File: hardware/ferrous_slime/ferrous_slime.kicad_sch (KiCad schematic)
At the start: 53 parts, among them J1 IMU_Connector, J2 Unused_IO, J3 Battery_Connector, J4 USB_C_Receptacle_USB2.0, Q1 CJ2305, SW1 SW_PWR, U1 BNO/MPU/ICM_Break, U2 ESP32-C3-MINI-1, U3 TP4056, U4 M3406, Y1 32.768Hz

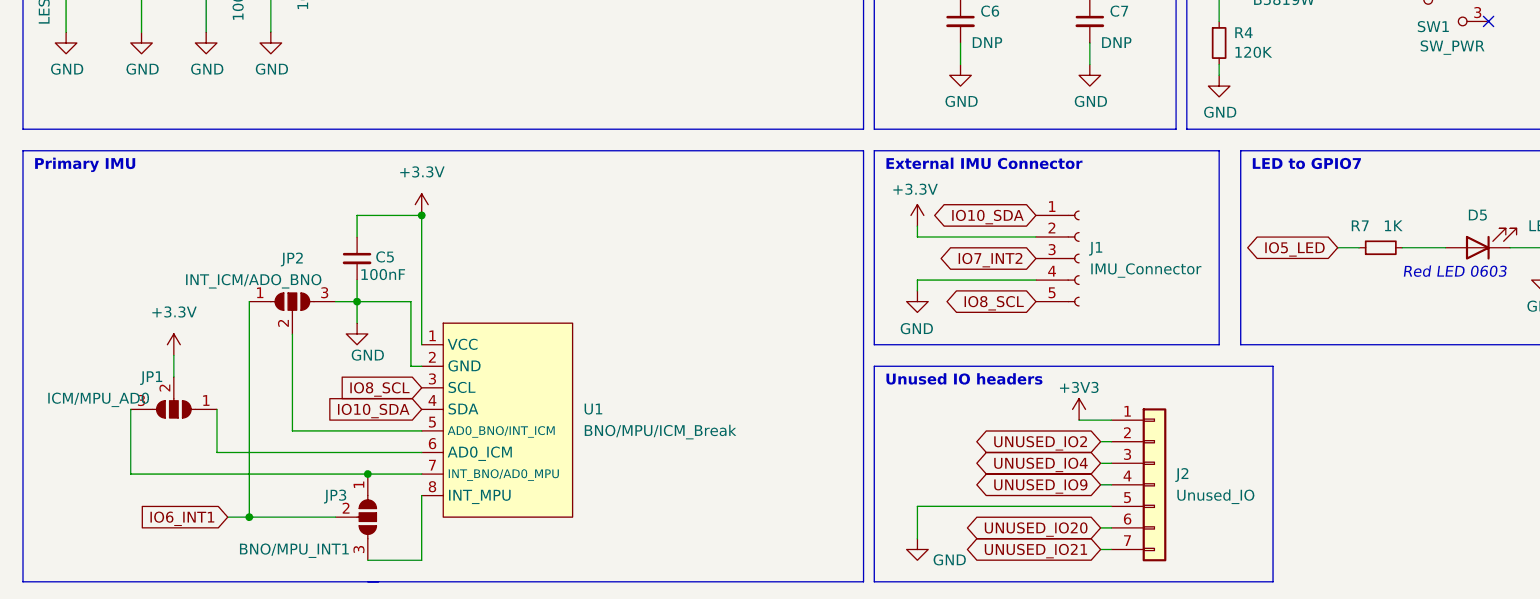
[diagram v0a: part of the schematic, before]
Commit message: Updated PCB to add second power pin
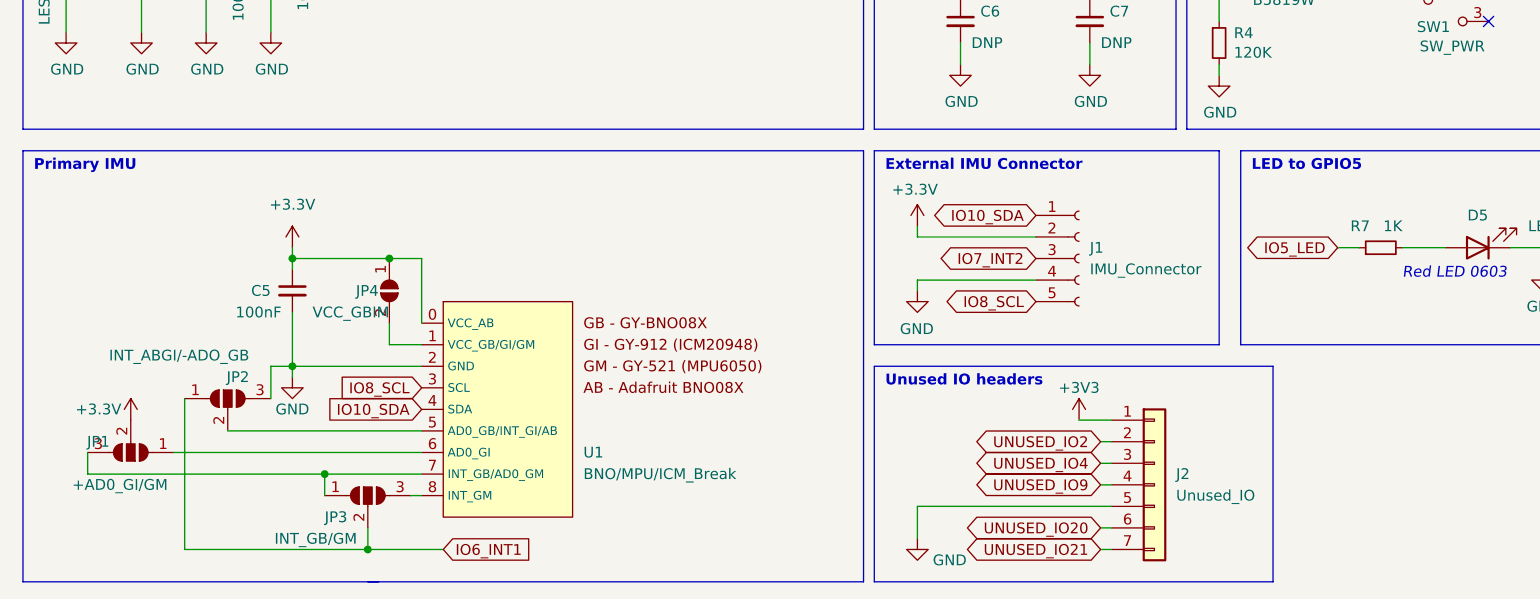
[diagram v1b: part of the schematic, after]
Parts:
- added JP4: VCC_GBIM, symbol Jumper:SolderJumper_2_Open
- JP1: value ICM/MPU_AD0 -> +AD0_GI/GM
- JP2: value INT_ICM/ADO_BNO -> INT_ABGI/-ADO_GB
- JP3: value BNO/MPU_INT1 -> INT_GB/GM
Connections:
- net +3V3: now also U1.0 (VCC_AB), JP4.1 (A); no longer U1.1 (VCC)
- new net: JP4.2 (B), U1.1 (VCC_GB/GI/GM)
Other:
- note added: "LED to GPIO5"
- note removed: "LED to GPIO7"
- moved on the sheet: C5, JP1, JP2, JP3

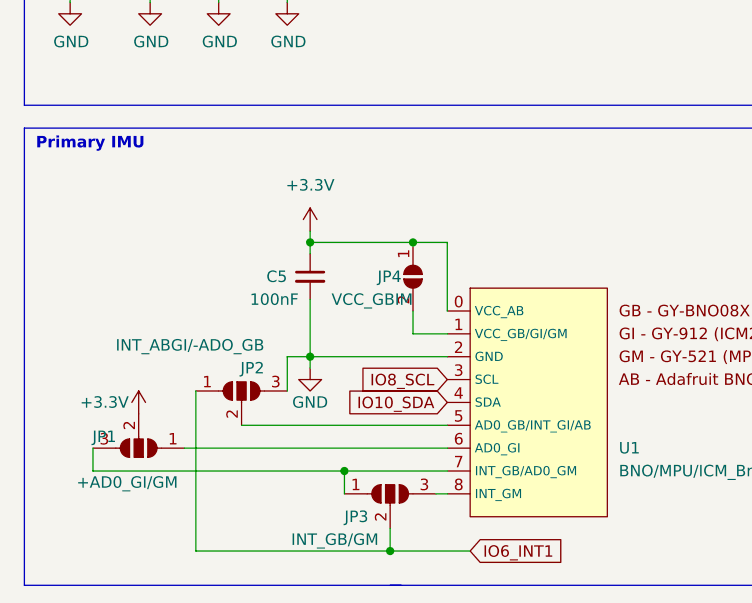
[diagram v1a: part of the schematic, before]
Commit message: Added adafruit bno to footprint
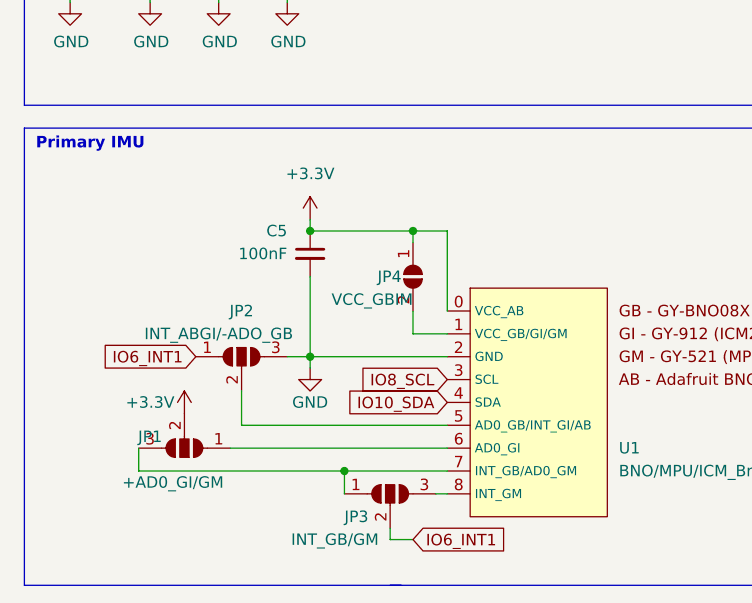
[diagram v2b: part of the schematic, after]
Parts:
- U1: footprint slimevr_pcb:BNO_MPU_ICM_Breakout -> slimevr_pcb:AB_GB_GM_GI_Breakout
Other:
- moved on the sheet: C5, JP1, JP2

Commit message: Finished pcb for ferrous_slime v0.2.0
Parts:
- D3: value LED_CHRG -> CHRG
- D4: value LED_FULL -> FULL
- D5: value LED -> LED_IO5
- JP4: footprint (none) -> Jumper:SolderJumper-2_P1.3mm_Open_RoundedPad1.0x1.5mm
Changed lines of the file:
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@@
   (title_block
     (title "ferrous_slime")
-    (date "2022-03-15")
+    (date "2022-10-11")
     (rev "v0.2.0")
     (company "github.com/thebutlah/slimevr_pcb")
@@
     (in_bom yes) (on_board yes)
     (property "Reference" "D5" (id 0) (at 185.42 121.92 0))
-    (property "Value" "LED" (id 1) (at 193.04 123.19 0))
+    (property "Value" "LED_IO5" (id 1) (at 191.77 121.92 0))
     (property "Footprint" "LED_SMD:LED_0603_1608Metric" (id 2) (at 185.42 125.73 0)
       (effects (font (size 1.27 1.27)) hide)
@@
       (effects (font (size 1.27 1.27)) (justify right))
     )
-    (property "Footprint" "" (id 2) (at 57.15 130.81 0)
+    (property "Footprint" "Jumper:SolderJumper-2_P1.3mm_Open_RoundedPad1.0x1.5mm" (id 2) (at 57.15 130.81 0)
       (effects (font (size 1.27 1.27)) hide)
     )
@@
     (in_bom yes) (on_board yes)
     (property "Reference" "D4" (id 0) (at 175.5021 40.5984 0))
-    (property "Value" "LED_FULL" (id 1) (at 179.07 44.45 0))
+    (property "Value" "FULL" (id 1) (at 181.61 40.64 0))
     (property "Footprint" "LED_SMD:LED_0603_1608Metric" (id 2) (at 177.8 41.91 90)
       (effects (font (size 1.27 1.27)) hide)
@@
     (in_bom yes) (on_board yes)
     (property "Reference" "D3" (id 0) (at 175.5021 35.4571 0))
-    (property "Value" "LED_CHRG" (id 1) (at 182.88 34.29 0))
+    (property "Value" "CHRG" (id 1) (at 181.61 35.56 0))
     (property "Footprint" "LED_SMD:LED_0603_1608Metric" (id 2) (at 177.8 36.83 90)
       (effects (font (size 1.27 1.27)) hide)
@@
     )
     (path "/bfab8950-194d-4203-9e99-e2292d8b3e2e"
-      (reference "D3") (unit 1) (value "LED_CHRG") (footprint "LED_SMD:LED_0603_1608Metric")
+      (reference "D3") (unit 1) (value "CHRG") (footprint "LED_SMD:LED_0603_1608Metric")
     )
     (path "/54080e1b-7a3e-4f86-8476-a3d55de881ec"
-      (reference "D4") (unit 1) (value "LED_FULL") (footprint "LED_SMD:LED_0603_1608Metric")
+      (reference "D4") (unit 1) (value "FULL") (footprint "LED_SMD:LED_0603_1608Metric")
     )
     (path "/00000000-0000-0000-0000-000061fd2211"
-      (reference "D5") (unit 1) (value "LED") (footprint "LED_SMD:LED_0603_1608Metric")
+      (reference "D5") (unit 1) (value "LED_IO5") (footprint "LED_SMD:LED_0603_1608Metric")
     )
     (path "/00000000-0000-0000-0000-0000625f4ff4"
@@
     )
     (path "/4b358e31-d2b1-4486-a811-6c8ba185f47e"
-      (reference "JP4") (unit 1) (value "VCC_GBIM") (footprint "")
+      (reference "JP4") (unit 1) (value "VCC_GBIM") (footprint "Jumper:SolderJumper-2_P1.3mm_Open_RoundedPad1.0x1.5mm")
     )
     (path "/32aeb981-ffe8-4bff-a65d-ee3788161f8a"

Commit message: ferrous_slime: v0.3.0
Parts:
- U1: value BNO/MPU/ICM_Break -> IMU_Breakout; footprint slimevr_pcb:AB_GB_GM_GI_Breakout -> slimevr_pcb:IMU_Breakout; symbol slimevr_pcb:BNO/MPU/ICM_Break -> slimevr_pcb:IMU_Breakout
- renumbered C8 to C7, C7 to C8, R3 to R2, R2 to R3
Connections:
- net +BATT: now also J3.1 (Pin_1); no longer J3.2 (Pin_2)
- net GND: now also J3.2 (Pin_2), U3.9 (EP); no longer J3.1 (Pin_1)
- net VBUS: no longer R3.2, U3.2 (PROG)
- new net: R3.2, U3.2 (PROG)
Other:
- note added: "R8 prevents ESD"
- note removed: "R12 prevents ESD"
- moved on the sheet: C7, R3

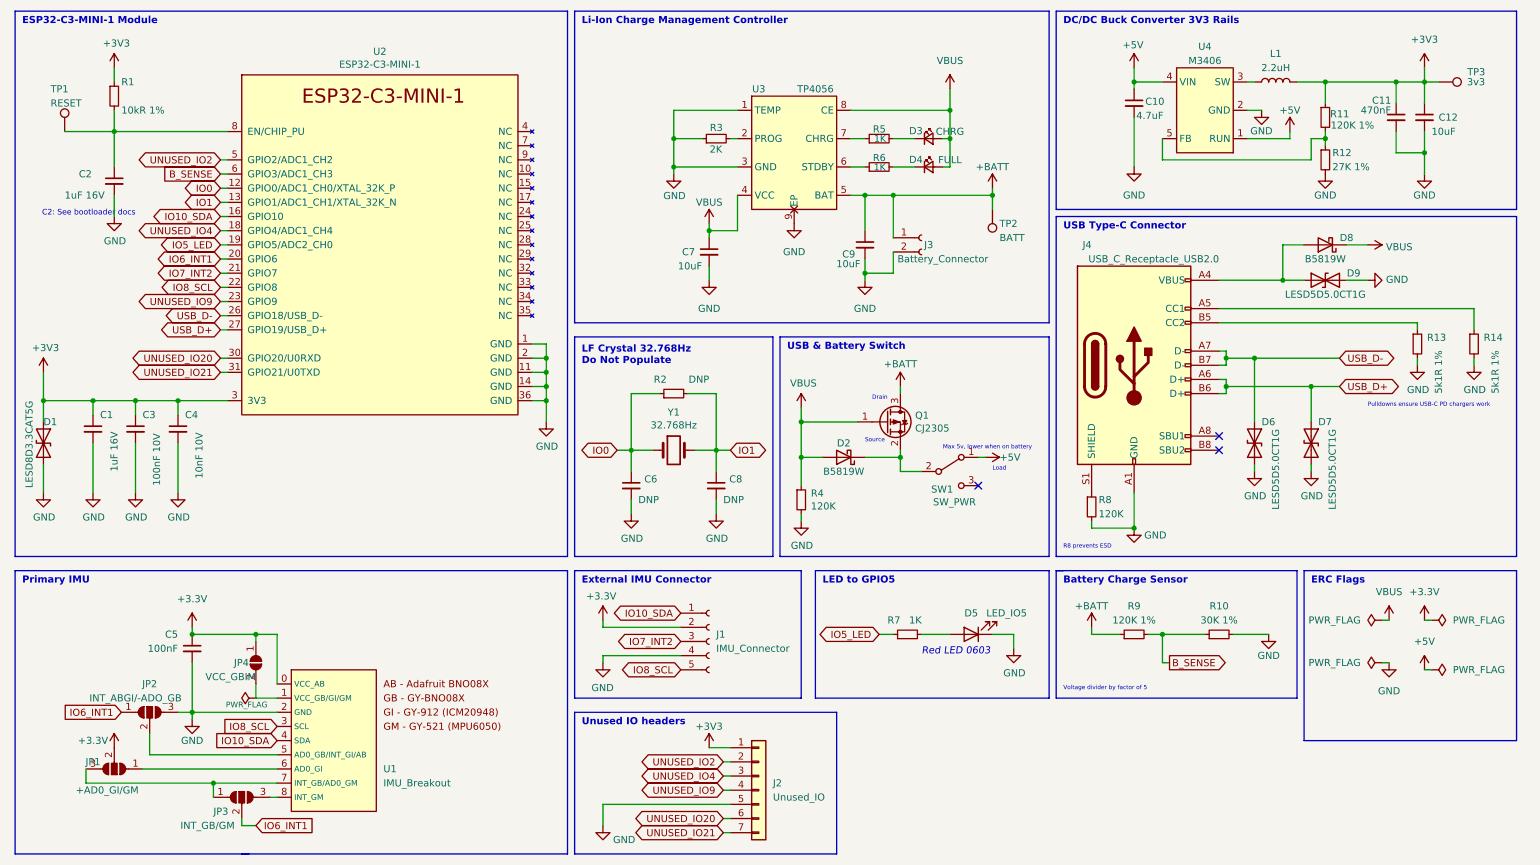
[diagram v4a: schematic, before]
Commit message: Now using srv05-4 and i2c pullups
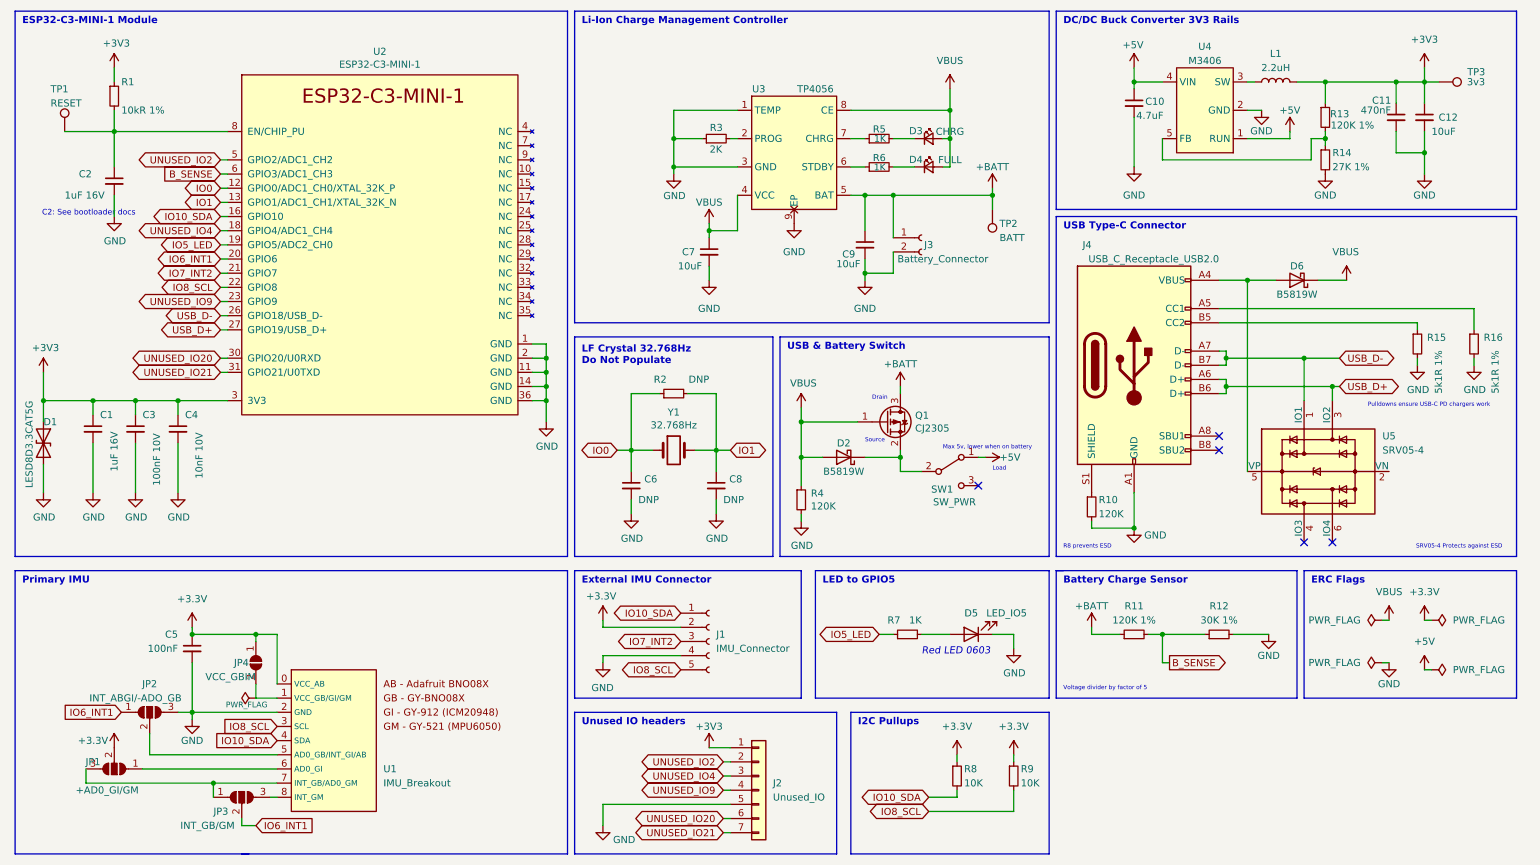
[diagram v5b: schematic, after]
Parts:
- removed D6, D7, D9: LESD5D5.0CT1G, Diode_SMD:D_SOD-523, symbol Device:D_TVS
- added R8, R9: 10K, Resistor_SMD:R_0603_1608Metric, symbol Device:R_Small
- added U5: SRV05-4, Package_TO_SOT_SMD:SOT-23-6, symbol Power_Protection:SRV05-4
- renumbered D8 to D6, R8 to R10, R9 to R11, R10 to R12, R11 to R13, R12 to R14, R13 to R15, R14 to R16
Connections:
- net +3V3: now also R8.1, R9.1
- net IO10_SDA: now also R8.2
- net IO8_SCL: now also R9.2
- net USB_D+: now also U5.3 (IO2)
- net USB_D-: now also U5.1 (IO1)
- net at D6.2 (A), J4.A4 (VBUS), J4.A9 (VBUS)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: now also U5.5 (VP)
- no-connect marks 3 -> 5
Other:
- note added: "I2C Pullups"
- note added: "SRV05-4 Protects against ESD"
- moved on the sheet: D6

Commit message: tmp
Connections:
- net GND: now also U5.2 (VN)
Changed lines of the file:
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@@
     (stroke (width 0) (type default) (color 0 0 0 0))
   )
+  (wire (pts (xy 260.35 96.52) (xy 262.89 96.52))
+    (stroke (width 0) (type default) (color 0 0 0 0))
+  )
   (wire (pts (xy 242.57 35.56) (xy 242.57 36.83))
     (stroke (width 0) (type default) (color 0 0 0 0))
@@
     (stroke (width 0) (type default) (color 0 0 0 0))
   )
+  (wire (pts (xy 262.89 96.52) (xy 262.89 99.06))
+    (stroke (width 0) (type default) (color 0 0 0 0))
+  )
   (wire (pts (xy 132.08 43.18) (xy 132.08 41.91))
     (stroke (width 0) (type default) (color 0 0 0 0))
@@
     (pin "1")
   )
+  (symbol (lib_id "power:GND") (at 262.89 99.06 0) (unit 1)
+    (in_bom yes) (on_board yes) (fields_autoplaced)
+    (property "Reference" "#PWR0101" (id 0) (at 262.89 105.41 0)
+      (effects (font (size 1.27 1.27)) hide)
+    )
+    (property "Value" "GND" (id 1) (at 262.89 104.14 0))
+    (property "Footprint" "" (id 2) (at 262.89 99.06 0)
+      (effects (font (size 1.27 1.27)) hide)
+    )
+    (property "Datasheet" "" (id 3) (at 262.89 99.06 0)
+      (effects (font (size 1.27 1.27)) hide)
+    )
+    (pin "1")
+  )
   (symbol (lib_id "Jumper:SolderJumper_3_Open") (at 31.75 149.86 180) (unit 1)
     (in_bom yes) (on_board yes)
@@
       (reference "#PWR048") (unit 1) (value "GND") (footprint "")
     )
+    (path "/c35dfe16-678b-43d7-adfd-5e876aafc041"
+      (reference "#PWR0101") (unit 1) (value "GND") (footprint "")
+    )
     (path "/00000000-0000-0000-0000-00006227c0fe"
